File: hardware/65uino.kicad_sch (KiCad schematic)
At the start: 38 parts, among them J1 Barrel_Jack_MountingPin, J2 USB_B_Micro, J3 OLED, SW1 RST, SW2 BTN, U1 R6507, U2 74HC04, U3 6532, U4 w27C512, U5 MIC5504-3.3YM5, U6 LM1117-5.0, Y1 1Mhz

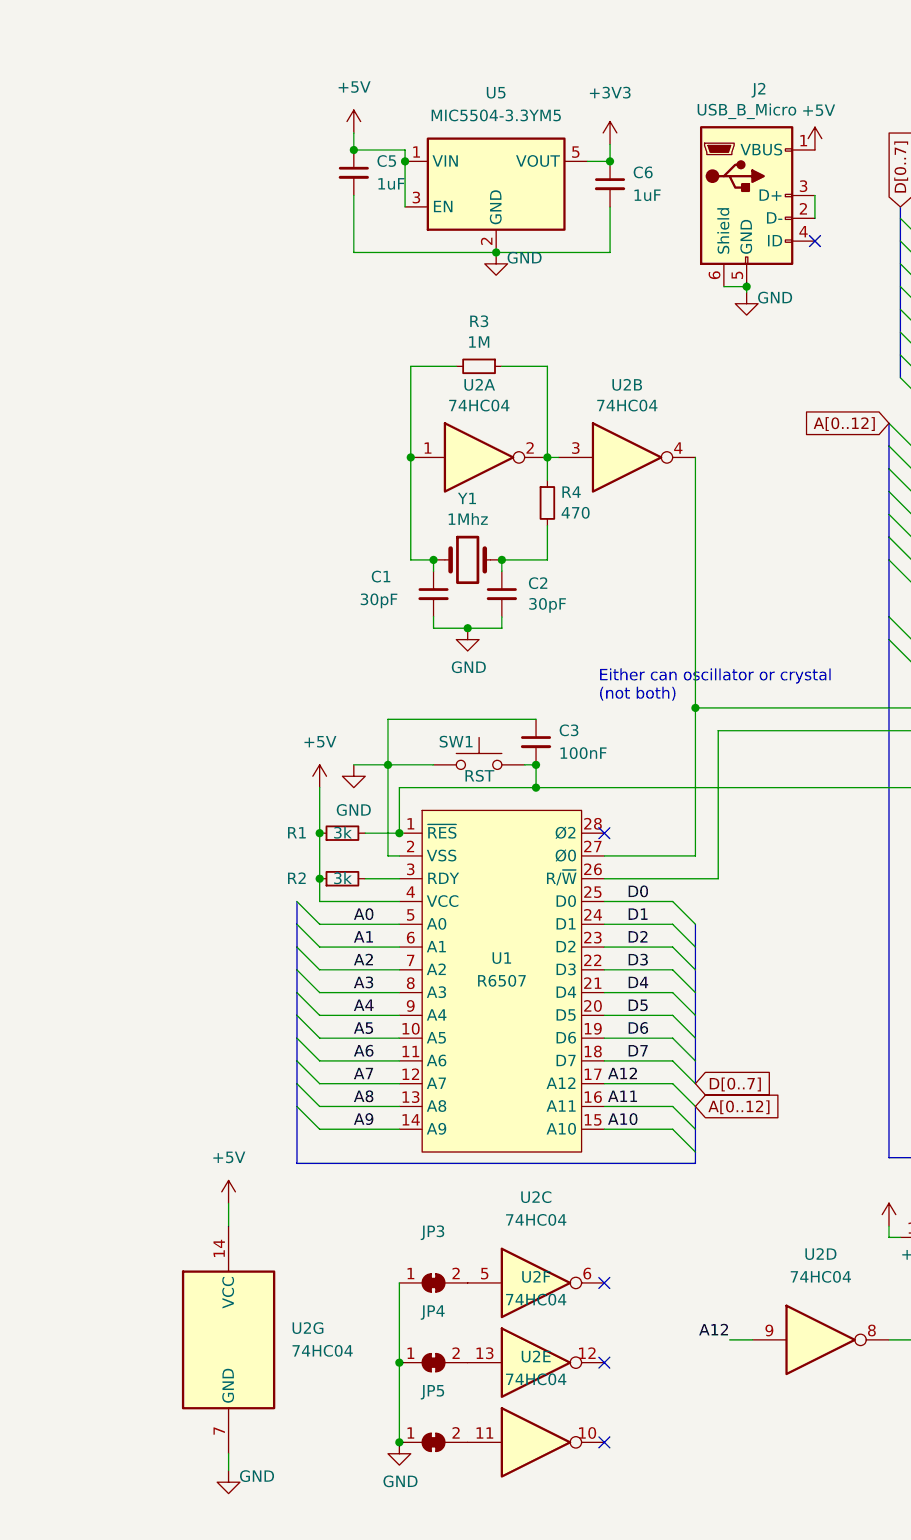
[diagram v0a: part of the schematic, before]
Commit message: Gerbers and SMD osc. added
First batch of PCB's ordered. Pads for an SMD oscillator added + extra decoupling pads.
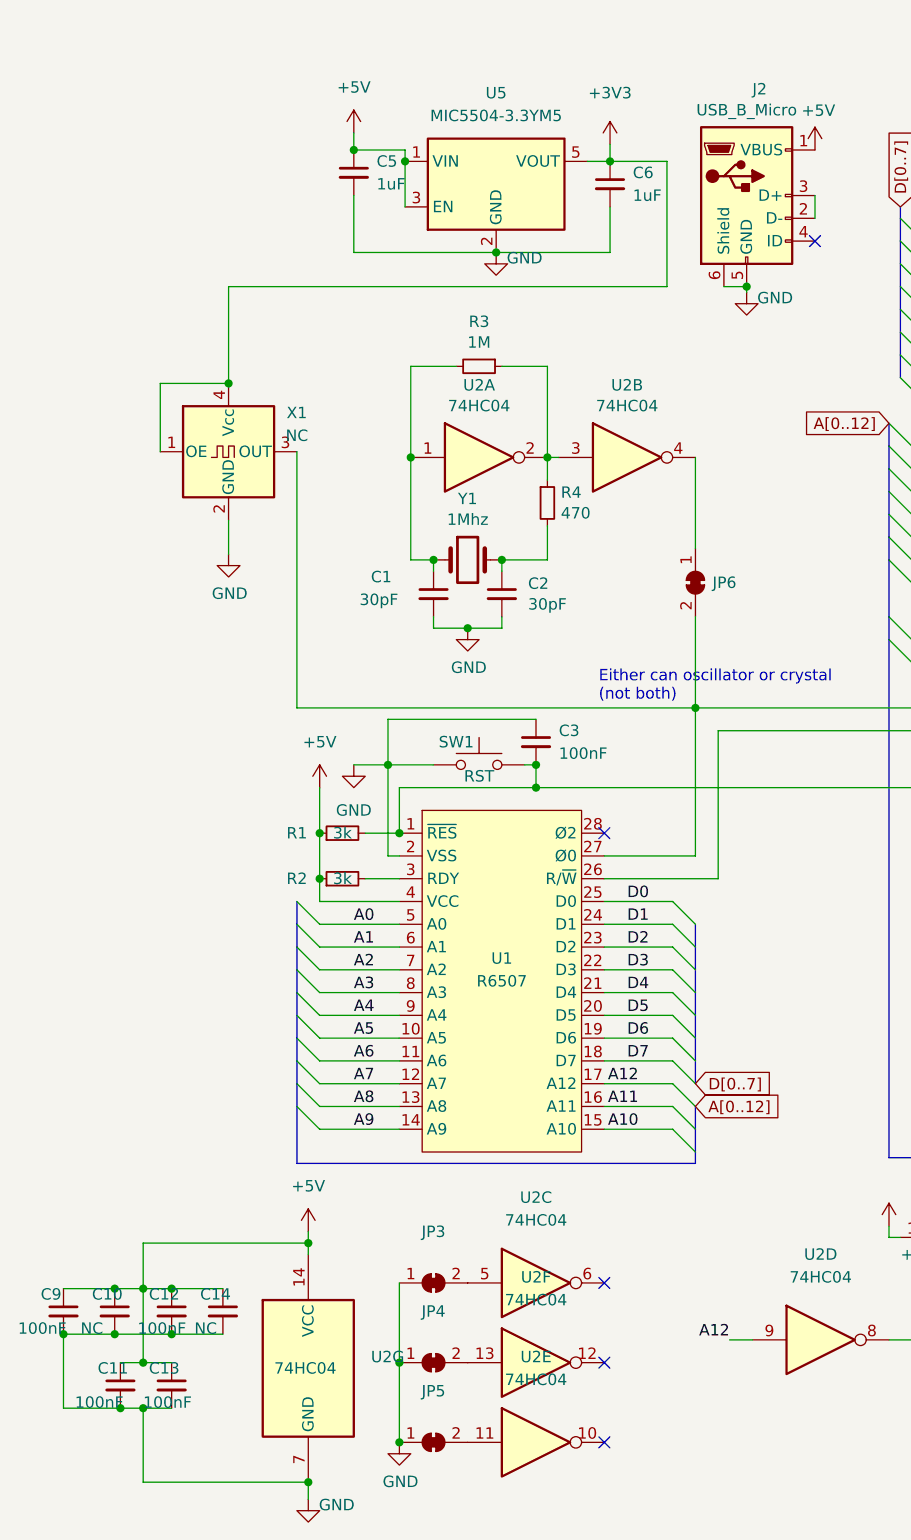
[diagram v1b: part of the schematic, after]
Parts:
- added C10, C14: NC, Capacitor_SMD:C_0805_2012Metric, symbol Device:C_Small
- added C11, C12, C13, C9: 100nF, Capacitor_SMD:C_0805_2012Metric, symbol Device:C_Small
- added JP6: SolderJumper_2_Bridged, Jumper:SolderJumper-2_P1.3mm_Bridged_RoundedPad1.0x1.5mm, symbol Jumper:SolderJumper_2_Bridged
- added X1: NC, Oscillator:Oscillator_SMD_SeikoEpson_SG210-4Pin_2.5x2.0mm_HandSoldering, symbol Oscillator:SG-210SCD
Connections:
- net +3V3: now also X1.1 (OE), X1.4 (Vcc)
- net +5V: now also C10.1, C11.1, C12.1, C13.1, C14.1, C9.1
- net GND: now also C10.2, C11.2, C12.2, C13.2, C14.2, C9.2, X1.2 (GND)
- net at U1.27 (Ø0), U3.39 (02): now also JP6.2 (B), X1.3 (OUT); no longer U2.4
- new net: JP6.1 (A), U2.4
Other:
- moved on the sheet: U2G

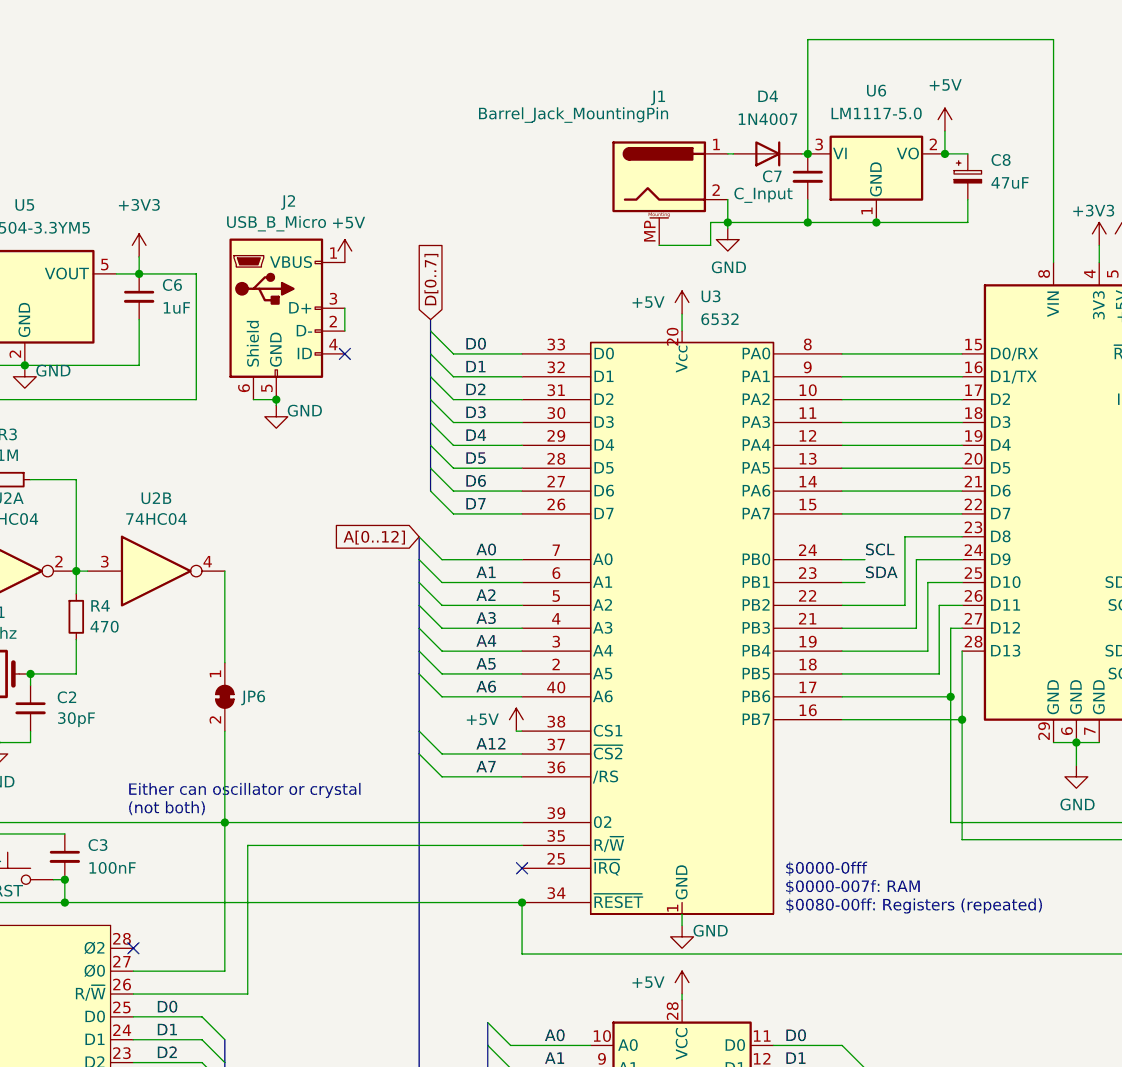
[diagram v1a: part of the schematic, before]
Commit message: Net names, silkscreen, software serial
Spoilers! :)
This has some hardware improvements but the gerber files haven't been updated this time (plot them from KiCAD).
There's also a spoiler for a future video: Software serial receives characters and outputs to screen.
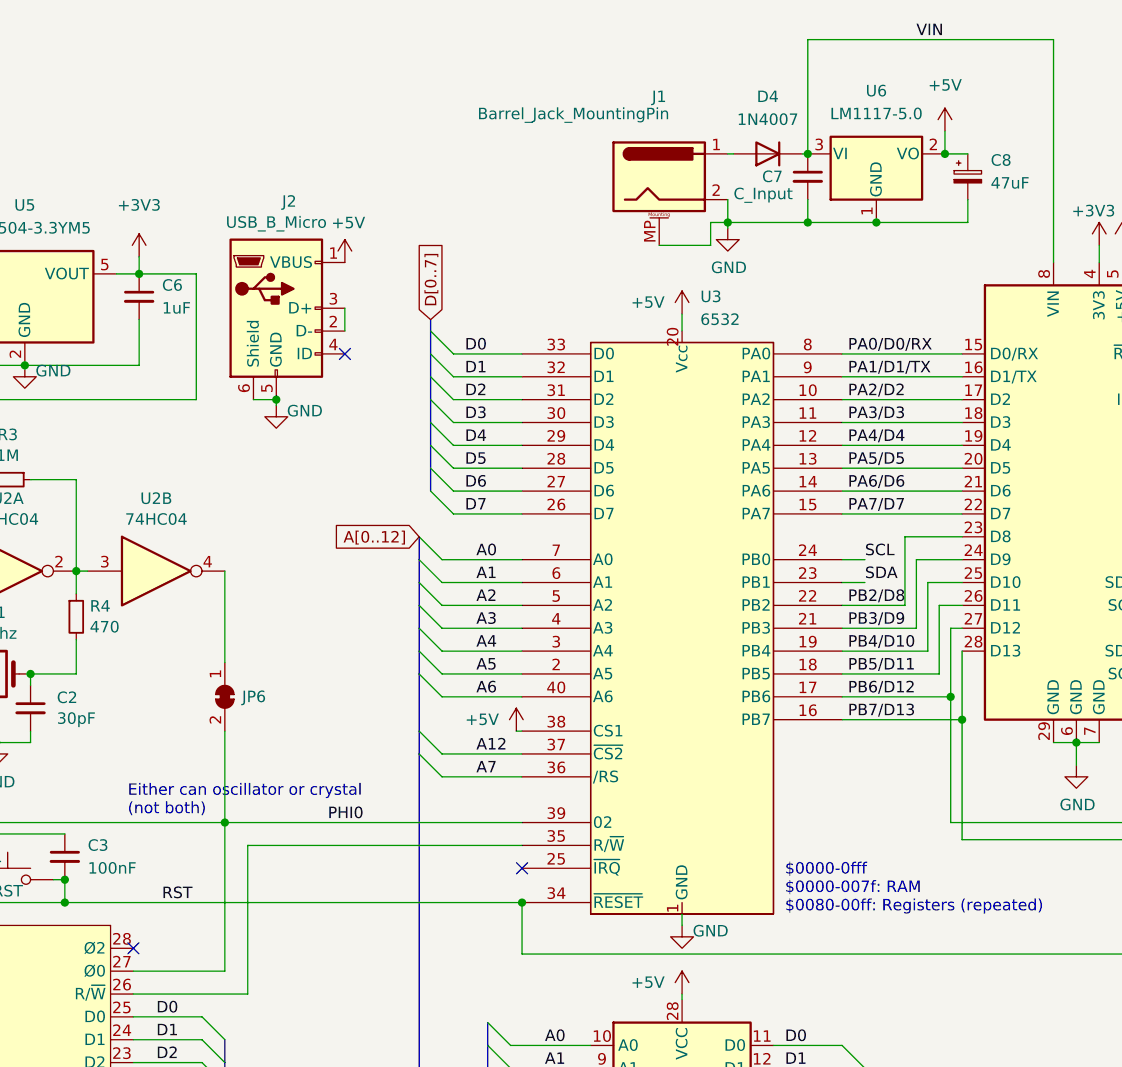
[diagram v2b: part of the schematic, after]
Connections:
- net PHI0: now reaches JP6.2 (B), U1.27 (Ø0), U3.39 (02), X1.3 (OUT)
- net RST: now reaches A1.3 (~{RESET}), C3.2, R1.2, SW1.2, U1.1 (~{RES}), U3.34 (~{RESET})
- net PB6/D12: now reaches A1.27 (D12), C4.1, R6.1, SW2.1, U3.17 (PB6)
- net VIN: now reaches A1.8 (VIN), C7.1, D4.1 (K), U6.3 (VI)
- net PA2/D2: now reaches A1.17 (D2), U3.10 (PA2)
- net PA3/D3: now reaches A1.18 (D3), U3.11 (PA3)
- net PA4/D4: now reaches A1.19 (D4), U3.12 (PA4)
- net PA5/D5: now reaches A1.20 (D5), U3.13 (PA5)
- net PA6/D6: now reaches A1.21 (D6), U3.14 (PA6)
- net PA7/D7: now reaches A1.22 (D7), U3.15 (PA7)
- net PB7/D13: now reaches A1.28 (D13), D1.1 (K), U3.16 (PB7)
- net PB5/D11: now reaches A1.26 (D11), U3.18 (PB5)
- net PB4/D10: now reaches A1.25 (D10), U3.19 (PB4)
- net PB3/D9: now reaches A1.24 (D9), U3.21 (PB3)
- net PB2/D8: now reaches A1.23 (D8), U3.22 (PB2)
- net PA0/D0/RX: now reaches A1.15 (D0/RX), U3.8 (PA0)
- net PA1/D1/TX: now reaches A1.16 (D1/TX), U3.9 (PA1)
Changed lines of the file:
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@@
+    (effects (font (size 1.27 1.27)) (justify left bottom))
+  )
+  (label "PB4{slash}D10" (at 156.845 86.36 0)
     (effects (font (size 1.27 1.27)) (justify left bottom))
   )
@@
     (effects (font (size 1.27 1.27)) (justify left bottom))
   )
+  (label "PB3{slash}D9" (at 156.845 83.82 0)
+    (effects (font (size 1.27 1.27)) (justify left bottom))
+  )
   (label "A6" (at 123.19 145.415 0)
     (effects (font (size 1.27 1.27)) (justify left bottom))
@@
     (effects (font (size 1.27 1.27)) (justify right bottom))
   )
+  (label "PB7{slash}D13" (at 156.845 93.98 0)
+    (effects (font (size 1.27 1.27)) (justify left bottom))
+  )
   (label "D4" (at 80.01 137.16 0)
     (effects (font (size 1.27 1.27)) (justify left bottom))
@@
     (effects (font (size 1.27 1.27)) (justify left bottom))
   )
+  (label "PA3{slash}D3" (at 156.845 60.96 0)
+    (effects (font (size 1.27 1.27)) (justify left bottom))
+  )
+  (label "PA4{slash}D4" (at 156.845 63.5 0)
+    (effects (font (size 1.27 1.27)) (justify left bottom))
+  )
   (label "A7" (at 123.19 147.955 0)
     (effects (font (size 1.27 1.27)) (justify left bottom))
@@
     (effects (font (size 1.27 1.27)) (justify left bottom))
   )
+  (label "PA5{slash}D5" (at 156.845 66.04 0)
+    (effects (font (size 1.27 1.27)) (justify left bottom))
+  )
+  (label "PA6{slash}D6" (at 156.845 68.58 0)
+    (effects (font (size 1.27 1.27)) (justify left bottom))
+  )
   (label "D0" (at 80.01 127 0)
     (effects (font (size 1.27 1.27)) (justify left bottom))
@@
     (effects (font (size 1.27 1.27)) (justify left bottom))
   )
+  (label "PA2{slash}D2" (at 156.845 58.42 0)
+    (effects (font (size 1.27 1.27)) (justify left bottom))
+  )
+  (label "PA0{slash}D0{slash}RX" (at 156.845 53.34 0)
+    (effects (font (size 1.27 1.27)) (justify left bottom))
+  )
   (label "A7" (at 115.57 100.33 0)
     (effects (font (size 1.27 1.27)) (justify left bottom))
@@
     (effects (font (size 1.27 1.27)) (justify left bottom))
   )
+  (label "PB5{slash}D11" (at 156.845 88.9 0)
+    (effects (font (size 1.27 1.27)) (justify left bottom))
+  )
+  (label "PHI0" (at 99.06 105.41 0)
+    (effects (font (size 1.27 1.27)) (justify left bottom))
+  )
   (label "A0" (at 123.19 130.175 0)
     (effects (font (size 1.27 1.27)) (justify left bottom))
@@
     (effects (font (size 1.27 1.27)) (justify left bottom))
   )
+  (label "PB6{slash}D12" (at 156.845 91.44 0)
+    (effects (font (size 1.27 1.27)) (justify left bottom))
+  )
   (label "A3" (at 115.57 83.82 0)
     (effects (font (size 1.27 1.27)) (justify left bottom))
@@
     (effects (font (size 1.27 1.27)) (justify left bottom))
   )
+  (label "PA7{slash}D7" (at 156.845 71.12 0)
+    (effects (font (size 1.27 1.27)) (justify left bottom))
+  )
   (label "A4" (at 49.53 139.7 0)
     (effects (font (size 1.27 1.27)) (justify left bottom))
@@
     (effects (font (size 1.27 1.27)) (justify left bottom))
   )
+  (label "PB2{slash}D8" (at 156.845 81.28 0)
+    (effects (font (size 1.27 1.27)) (justify left bottom))
+  )
   (label "A2" (at 115.57 81.28 0)
     (effects (font (size 1.27 1.27)) (justify left bottom))
@@
     (effects (font (size 1.27 1.27)) (justify left bottom))
   )
+  (label "PA1{slash}D1{slash}TX" (at 156.845 55.88 0)
+    (effects (font (size 1.27 1.27)) (justify left bottom))
+  )
   (label "D7" (at 80.01 144.78 0)
     (effects (font (size 1.27 1.27)) (justify left bottom))
@@
     (effects (font (size 1.27 1.27)) (justify left bottom))
   )
+  (label "RST" (at 80.645 114.3 0)
+    (effects (font (size 1.27 1.27)) (justify left bottom))
+  )
   (label "D5" (at 80.01 139.7 0)
     (effects (font (size 1.27 1.27)) (justify left bottom))
@@
     (effects (font (size 1.27 1.27)) (justify left bottom))
   )
+  (label "VIN" (at 164.465 18.415 0)
+    (effects (font (size 1.27 1.27)) (justify left bottom))
+  )
